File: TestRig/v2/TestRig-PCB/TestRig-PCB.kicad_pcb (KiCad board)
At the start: 2 copper layers, 15 parts, among them J201 DUT_CONN, U201 74LS165, U202 74LS165, U203 74LS165

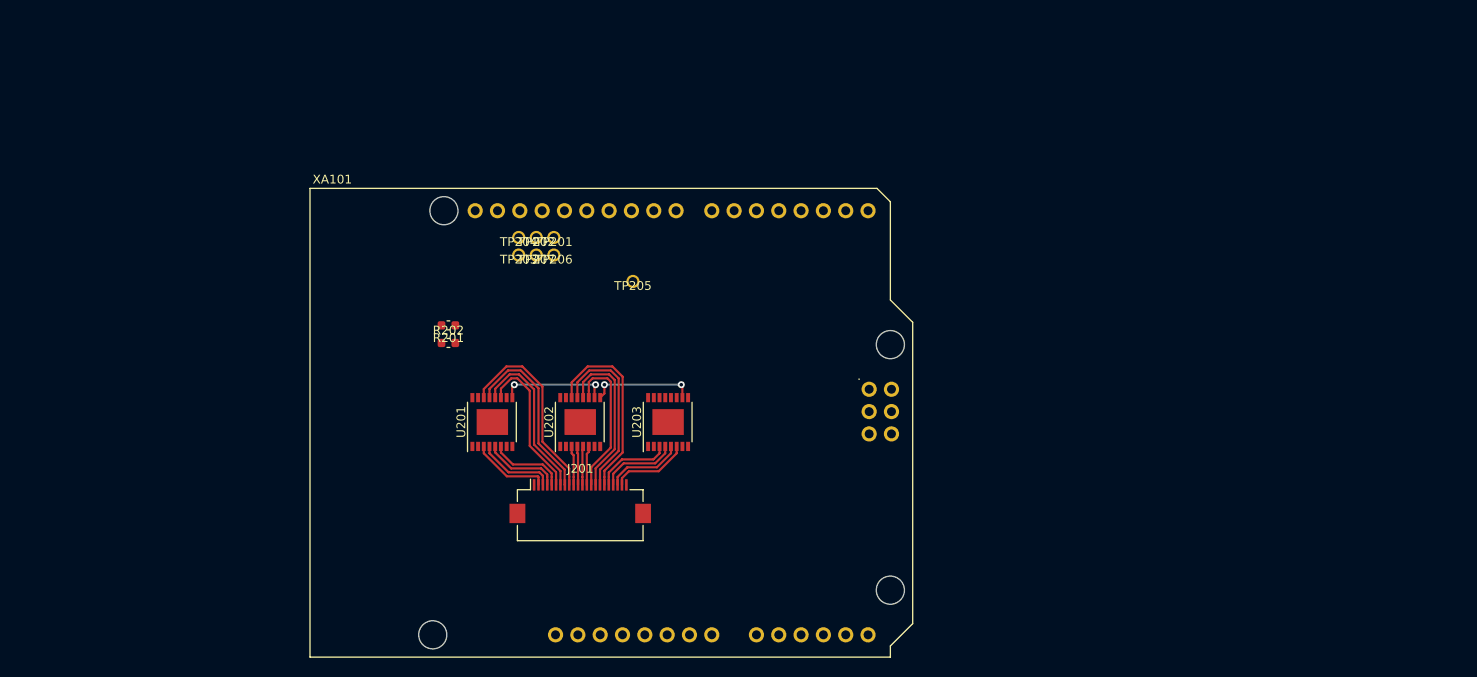
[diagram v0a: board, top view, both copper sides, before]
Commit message: Adds working test rig
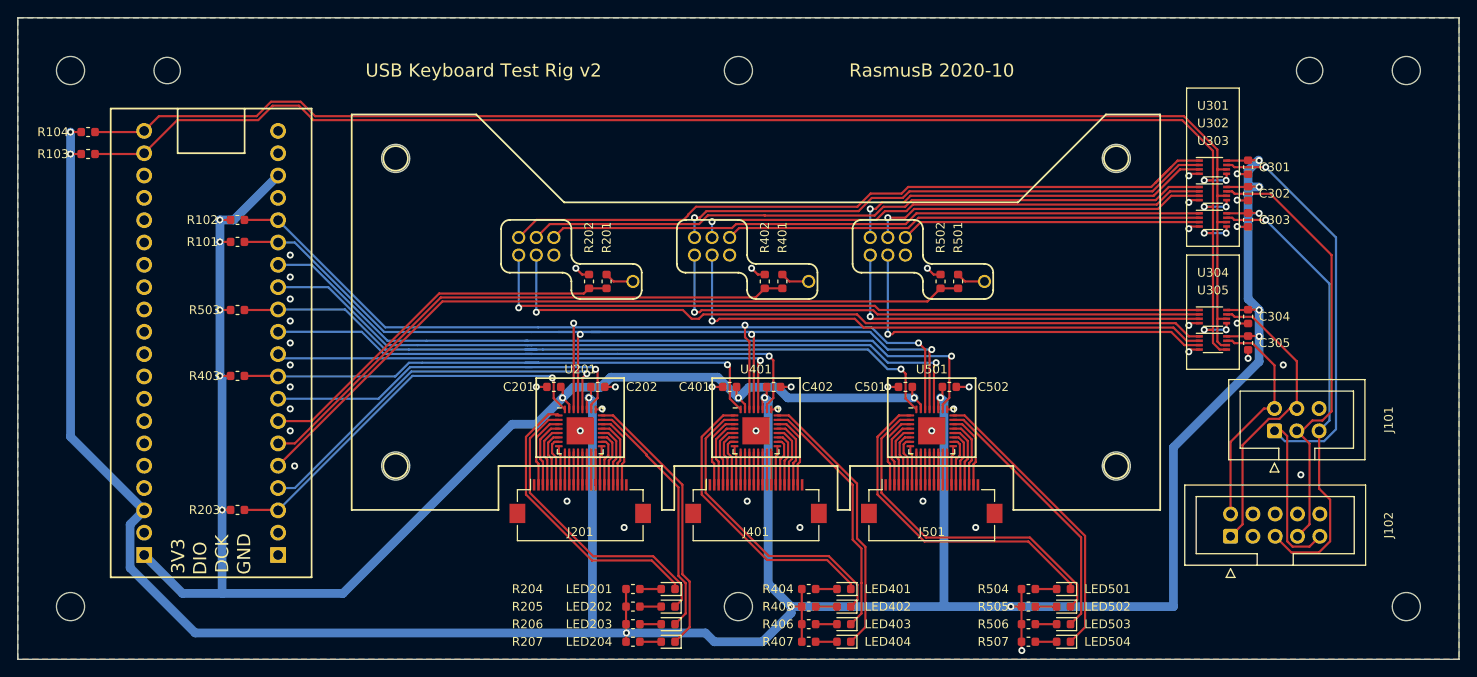
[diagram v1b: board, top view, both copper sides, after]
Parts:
- removed U202, U203: 74LS165, Package_SO:TSSOP-16-1EP_4.4x5mm_P0.65mm
- removed XA101: Arduino_Leonardo_Shield, USB-Keyboard:Arduino_Leonardo_Shield
- added C201: 100n, Capacitor_SMD:C_0603_1608Metric, F.Cu at (135.0, 92.0)
- added C202: 100n, Capacitor_SMD:C_0603_1608Metric, F.Cu at (140.0, 92.0)
- added C301: 100n, Capacitor_SMD:C_0603_1608Metric, F.Cu at (214.0, 67.0)
- added C302: 100n, Capacitor_SMD:C_0603_1608Metric, F.Cu at (214.0, 70.0)
- added C303: 100n, Capacitor_SMD:C_0603_1608Metric, F.Cu at (214.0, 73.0)
- added C304: 100n, Capacitor_SMD:C_0603_1608Metric, F.Cu at (214.0, 84.0)
- added C305: 100n, Capacitor_SMD:C_0603_1608Metric, F.Cu at (214.0, 87.0)
- added C401: 100n, Capacitor_SMD:C_0603_1608Metric, F.Cu at (155.0, 92.0)
- added C402: 100n, Capacitor_SMD:C_0603_1608Metric, F.Cu at (160.0, 92.0)
- added C501: 100n, Capacitor_SMD:C_0603_1608Metric, F.Cu at (175.0, 92.0)
- added C502: 100n, Capacitor_SMD:C_0603_1608Metric, F.Cu at (180.0, 92.0)
- added DUT401: DUT_OUTLINE, USB-Keyboard:USB_KEYBOARD_ADAPTER_V1.22_DUMMY, F.Cu at (149.0, 73.0)
- added DUT501: DUT_OUTLINE, USB-Keyboard:USB_KEYBOARD_ADAPTER_V1.22_DUMMY, F.Cu at (169.0, 73.0)
- added H101: M3, MountingHole:MountingHole_3.2mm_M3, F.Cu at (80.0, 56.0)
- added H102: M3, MountingHole:MountingHole_3.2mm_M3, F.Cu at (156.0, 56.0)
- added H103: M3, MountingHole:MountingHole_3.2mm_M3, F.Cu at (232.0, 56.0)
- added H104: M3, MountingHole:MountingHole_3.2mm_M3, F.Cu at (80.0, 117.0)
- added H105: M3, MountingHole:MountingHole_3.2mm_M3, F.Cu at (156.0, 117.0)
- added H106: M3, MountingHole:MountingHole_3.2mm_M3, F.Cu at (232.0, 117.0)
- added J101: AVR-ISP-6, Connector_IDC:IDC-Header_2x03_P2.54mm_Vertical, F.Cu at (217.0, 97.0)
- added J102: AVR-ISP-10, Connector_IDC:IDC-Header_2x05_P2.54mm_Vertical, F.Cu at (212.0, 109.0)
- added J401: DUT_CONN, Connector_FFC-FPC:Hirose_FH12-22S-0.5SH_1x22-1MP_P0.50mm_Horizontal, F.Cu at (158.0, 105.0)
- added J501: DUT_CONN, Connector_FFC-FPC:Hirose_FH12-22S-0.5SH_1x22-1MP_P0.50mm_Horizontal, F.Cu at (178.0, 105.0)
- added JIG_OUTLINE_1: TEST_JIG, USB-Keyboard:TestJig, F.Cu at (112.0, 106.0)
- added LED201: RED, LED_SMD:LED_0603_1608Metric, F.Cu at (148.0, 115.0)
- added LED202: ORNG, LED_SMD:LED_0603_1608Metric, F.Cu at (148.0, 117.0)
- added LED203: YLW, LED_SMD:LED_0603_1608Metric, F.Cu at (148.0, 119.0)
- added LED204: GRN, LED_SMD:LED_0603_1608Metric, F.Cu at (148.0, 121.0)
- added LED401: RED, LED_SMD:LED_0603_1608Metric, F.Cu at (168.0, 115.0)
- added LED402: ORNG, LED_SMD:LED_0603_1608Metric, F.Cu at (168.0, 117.0)
- added LED403: YLW, LED_SMD:LED_0603_1608Metric, F.Cu at (168.0, 119.0)
- added LED404: GRN, LED_SMD:LED_0603_1608Metric, F.Cu at (168.0, 121.0)
- added LED501: RED, LED_SMD:LED_0603_1608Metric, F.Cu at (193.0, 115.0)
- added LED502: ORNG, LED_SMD:LED_0603_1608Metric, F.Cu at (193.0, 117.0)
- added LED503: YLW, LED_SMD:LED_0603_1608Metric, F.Cu at (193.0, 119.0)
- added LED504: GRN, LED_SMD:LED_0603_1608Metric, F.Cu at (193.0, 121.0)
- added MOD101: STM32_BLUE_PILL, BluePill:STM32F103C8T6-ARM-BOARD, F.Cu at (96.0, 87.0)
- added R101: 4k7, Resistor_SMD:R_0603_1608Metric, F.Cu at (99.0, 75.5)
- added R102: 4k7, Resistor_SMD:R_0603_1608Metric, F.Cu at (99.0, 73.0)
- added R103: 10k, Resistor_SMD:R_0603_1608Metric, F.Cu at (82.0, 65.5)
- added R104: 10k, Resistor_SMD:R_0603_1608Metric, F.Cu at (82.0, 63.0)
- added R203: 4k7, Resistor_SMD:R_0603_1608Metric, F.Cu at (99.0, 106.0)
- added R204: 270R, Resistor_SMD:R_0603_1608Metric, F.Cu at (144.0, 115.0)
- added R205: 270R, Resistor_SMD:R_0603_1608Metric, F.Cu at (144.0, 117.0)
- added R206: 270R, Resistor_SMD:R_0603_1608Metric, F.Cu at (144.0, 119.0)
- added R207: 270R, Resistor_SMD:R_0603_1608Metric, F.Cu at (144.0, 121.0)
- added R401: 10k 1%, Resistor_SMD:R_0603_1608Metric, F.Cu at (161.0, 80.0)
- added R402: 10k 1%, Resistor_SMD:R_0603_1608Metric, F.Cu at (159.0, 80.0)
- added R403: 4k7, Resistor_SMD:R_0603_1608Metric, F.Cu at (99.0, 90.8)
- added R404: 270R, Resistor_SMD:R_0603_1608Metric, F.Cu at (164.0, 115.0)
- added R405: 270R, Resistor_SMD:R_0603_1608Metric, F.Cu at (164.0, 117.0)
- added R406: 270R, Resistor_SMD:R_0603_1608Metric, F.Cu at (164.0, 119.0)
- added R407: 270R, Resistor_SMD:R_0603_1608Metric, F.Cu at (164.0, 121.0)
- added R501: 10k 1%, Resistor_SMD:R_0603_1608Metric, F.Cu at (181.0, 80.0)
- added R502: 10k 1%, Resistor_SMD:R_0603_1608Metric, F.Cu at (179.0, 80.0)
- added R503: 4k7, Resistor_SMD:R_0603_1608Metric, F.Cu at (99.0, 83.2)
- added R504: 270R, Resistor_SMD:R_0603_1608Metric, F.Cu at (189.0, 115.0)
- added R505: 270R, Resistor_SMD:R_0603_1608Metric, F.Cu at (189.0, 117.0)
- added R506: 270R, Resistor_SMD:R_0603_1608Metric, F.Cu at (189.0, 119.0)
- added R507: 270R, Resistor_SMD:R_0603_1608Metric, F.Cu at (189.0, 121.0)
- added REG101: eC_REG, PCB Extras:eC-Registration, F.Cu at (91.0, 56.0)
- added REG102: eC_REG, PCB Extras:eC-Registration, F.Cu at (221.0, 56.0)
- added TP401: RESET, Pogo:Pogo_P50_Bottom, F.Cu at (155.0, 75.0)
- added TP402: SCK, Pogo:Pogo_P50_Bottom, F.Cu at (153.0, 75.0)
- added TP403: MOSI, Pogo:Pogo_P50_Bottom, F.Cu at (151.0, 77.0)
- added TP404: MISO, Pogo:Pogo_P50_Bottom, F.Cu at (151.0, 75.0)
- added TP405: VTARGET, Pogo:Pogo_P50_Bottom, F.Cu at (153.0, 77.0)
- added TP406: VBUS, Pogo:Pogo_P50_Bottom, F.Cu at (164.0, 80.0)
- added TP407: GND, Pogo:Pogo_P50_Bottom, F.Cu at (155.0, 77.0)
- added TP501: RESET, Pogo:Pogo_P50_Bottom, F.Cu at (175.0, 75.0)
- added TP502: SCK, Pogo:Pogo_P50_Bottom, F.Cu at (173.0, 75.0)
- added TP503: MOSI, Pogo:Pogo_P50_Bottom, F.Cu at (171.0, 77.0)
- added TP504: MISO, Pogo:Pogo_P50_Bottom, F.Cu at (171.0, 75.0)
- added TP505: VTARGET, Pogo:Pogo_P50_Bottom, F.Cu at (173.0, 77.0)
- added TP506: VBUS, Pogo:Pogo_P50_Bottom, F.Cu at (184.0, 80.0)
- added TP507: GND, Pogo:Pogo_P50_Bottom, F.Cu at (175.0, 77.0)
- added U301: TS5A3357, Package_SO:VSSOP-8_2.3x2mm_P0.5mm, F.Cu at (210.0, 67.0)
- added U302: TS5A3357, Package_SO:VSSOP-8_2.3x2mm_P0.5mm, F.Cu at (210.0, 70.0)
- added U303: TS5A3357, Package_SO:VSSOP-8_2.3x2mm_P0.5mm, F.Cu at (210.0, 73.0)
- added U304: TS5A3357, Package_SO:VSSOP-8_2.3x2mm_P0.5mm, F.Cu at (210.0, 84.0)
- added U305: TS5A3357, Package_SO:VSSOP-8_2.3x2mm_P0.5mm, F.Cu at (210.0, 87.0)
- added U401: TCA6424A, Package_DFN_QFN:QFN-32-1EP_5x5mm_P0.5mm_EP3.1x3.1mm, F.Cu at (158.0, 97.0)
- added U501: TCA6424A, Package_DFN_QFN:QFN-32-1EP_5x5mm_P0.5mm_EP3.1x3.1mm, F.Cu at (178.0, 97.0)
- DUT201: moved to F.Cu
- R201, R202: value R_Small -> 10k 1%
- TP205: value VBUS -> VTARGET
- TP206: value GND -> VBUS
- TP207: value VTARGET -> GND
- U201: value 74LS165 -> TCA6424A; footprint Package_SO:TSSOP-16-1EP_4.4x5mm_P0.65mm -> Package_DFN_QFN:QFN-32-1EP_5x5mm_P0.5mm_EP3.1x3.1mm
- moved R201 18.7 mm to (141.0, 80.0), turned to 270 degrees
- moved R202 17.5 mm to (139.0, 80.0), turned to 90 degrees
- moved TP205 11.4 mm to (133.0, 77.0)
- moved U201 10.0 mm to (138.0, 97.0), turned to 0 degrees
- moved TP206 9.49 mm to (144.0, 80.0)
- moved TP207 2.00 mm to (135.0, 77.0)
- turned DUT201 to 270 degrees
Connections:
- net /DUT 1/DUT_VBUS renamed /uA_DUT1_VBUS
- TP201 pad 1: /DUT 1/ICSP_RESET -> /ISP Multiplexer/DUT1_ISP_RESET
- TP202 pad 1: /DUT 1/ICSP_SCK -> /ISP Multiplexer/DUT1_ISP_CLK
- TP203 pad 1: /DUT 1/ICSP_MOSI -> /ISP Multiplexer/DUT1_ISP_MOSI
- TP204 pad 1: /DUT 1/ICSP_MISO -> /ISP Multiplexer/DUT1_ISP_MISO
- TP205 pad 1: Net-(R201-Pad1) -> /ISP Multiplexer/DUT1_ISP_VTARGET
- TP206 pad 1: GND -> Net-(R201-Pad1)
- TP207 pad 1: /DUT 1/ICSP_VTARGET -> GND
- U201 pad 1: /DUT 1/~SR_PL -> Net-(LED201-Pad1)
- U201 pad 10: /DUT 1/SR_DI -> /DUT 1/KB_09
- U201 pad 11: /DUT 1/KB_06 -> /DUT 1/KB_10
- U201 pad 12: /DUT 1/KB_07 -> /DUT 1/KB_11
- U201 pad 13: /DUT 1/KB_08 -> /DUT 1/KB_12
- U201 pad 14: /DUT 1/KB_09 -> /DUT 1/KB_13
- U201 pad 15: /DUT 1/~SR_CE -> /DUT 1/KB_14
- U201 pad 16: Net-(U201-Pad16) -> /DUT 1/KB_15
- U201 pad 17: (no net) -> /DUT 1/KB_16
- U201 pad 2: /DUT 1/SR_CP -> Net-(LED202-Pad1)
- U201 pad 7: Net-(U201-Pad7) -> /DUT 1/KB_06
- U201 pad 8: GND -> /DUT 1/KB_07
- U201 pad 9: Net-(U201-Pad9) -> /DUT 1/KB_08
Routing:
- net +5V: track 0.00 -> 363.8 mm, vias 0 -> 14
- net /ISP Multiplexer/DUT_SEL_2: track 0.00 -> 172.4 mm, vias 0 -> 8
- net +3V3: track 0.00 -> 168.6 mm, vias 0 -> 8
- net /ISP Multiplexer/DUT_SEL_1: track 0.00 -> 158.7 mm
- net /I2C_SCL: track 0.00 -> 144.6 mm, vias 0 -> 3
- net /I2C_SDA: track 0.00 -> 110.8 mm, vias 0 -> 3
- net /DUT3_I2C_ADDR: track 0.00 -> 87.7 mm, vias 0 -> 1
- net /uA_DUT3_VBUS: track 0.00 -> 85.7 mm
- net /DUT3_I2C_~RESET: track 0.00 -> 84.6 mm, vias 0 -> 1
- net /DUT3_I2C_~INT: track 0.00 -> 84.1 mm, vias 0 -> 1
- net /ISP Multiplexer/DUT1_ISP_MOSI: track 0.00 -> 83.7 mm, vias 0 -> 1
- net /ISP Multiplexer/DUT1_ISP_VTARGET: track 0.00 -> 83.7 mm, vias 0 -> 1
- net /ISP Multiplexer/DUT1_ISP_MISO: track 0.00 -> 83.6 mm
- net /ISP Multiplexer/DUT1_ISP_CLK: track 0.00 -> 77.9 mm
- net /ISP Multiplexer/DUT1_ISP_RESET: track 0.00 -> 74.6 mm
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- added copper zone on B.Cu, net GND
- added copper zone on F.Cu, net GND
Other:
- board outline added: 164 x 73 mm
- board text added: "RasmusB 2020-10"
- board text added: "USB Keyboard Test Rig v2"
